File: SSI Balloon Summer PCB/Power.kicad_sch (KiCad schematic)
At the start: 35 parts, among them J1 Battery connector, Q2 DMG2305UX-7, SW1 SW_SPDT, U11 TPS63070RNMR, U12 TPS63070RNMR, U3 AP2112K-3.3TRG1

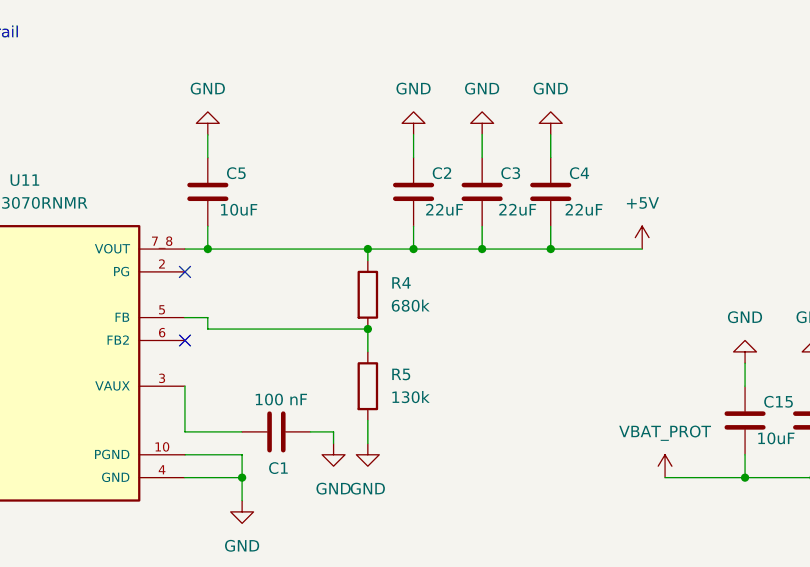
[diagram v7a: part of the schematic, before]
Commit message: Removed sketchy R4 footprint
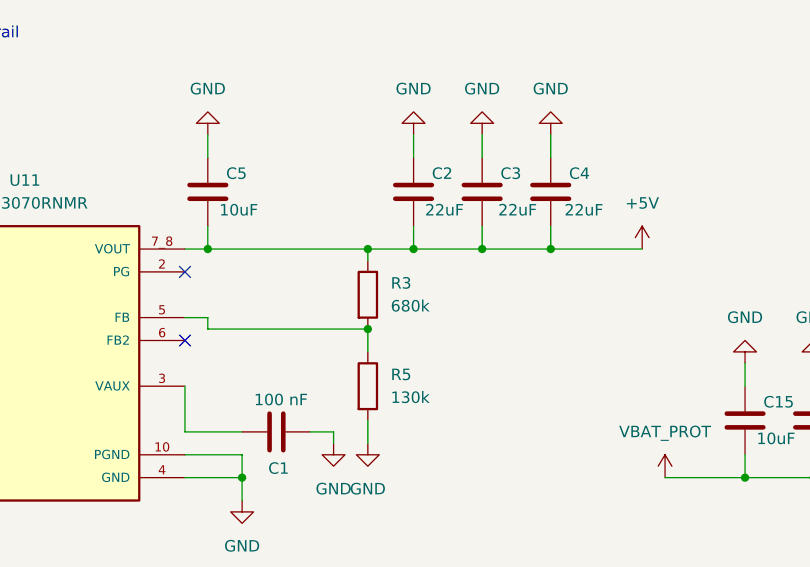
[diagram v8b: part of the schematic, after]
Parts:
- removed R4: 680k, AP2112K-3.3TRG1:SOT95P285X140-5N, symbol Device:R
- added R3: 680k, Resistor_SMD:R_0603_1608Metric, symbol Device:R
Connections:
- net +5V: now also R3.1
- net at R5.1, U11.5 (FB): now also R3.2
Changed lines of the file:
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@@
+	)
+	(junction
+		(at 120.65 102.87)
+		(diameter 0)
+		(color 0 0 0 0)
 	)
 	(junction
 		(at 233.68 144.78)
-		(diameter 0)
-		(color 0 0 0 0)
-	)
-	(junction
-		(at 120.65 102.87)
 		(diameter 0)
 		(color 0 0 0 0)
@@
 	)
 	(symbol
+		(lib_id "Device:R")
+		(at 120.65 99.06 0)
+		(unit 1)
+		(body_style 1)
+		(exclude_from_sim no)
+		(in_bom yes)
+		(on_board yes)
+		(in_pos_files yes)
+		(dnp no)
+		(fields_autoplaced yes)
+		(property "Reference" "R3"
+			(at 123.19 97.7899 0)
+			(show_name no)
+			(do_not_autoplace no)
+			(effects
+				(font
+					(size 1.27 1.27)
+				)
+				(justify left)
+			)
+		)
+		(property "Value" "680k"
+			(at 123.19 100.3299 0)
+			(show_name no)
+			(do_not_autoplace no)
+			(effects
+				(font
+					(size 1.27 1.27)
+				)
+				(justify left)
+			)
+		)
+		(property "Footprint" "Resistor_SMD:R_0603_1608Metric"
+			(at 118.872 99.06 90)
+			(hide yes)
+			(show_name no)
+			(do_not_autoplace no)
+			(effects
+				(font
+					(size 1.27 1.27)
+				)
+			)
+		)
+		(property "Datasheet" ""
+			(at 120.65 99.06 0)
+			(hide yes)
+			(show_name no)
+			(do_not_autoplace no)
+			(effects
+				(font
+					(size 1.27 1.27)
+				)
+			)
+		)
+		(property "Description" "Resistor"
+			(at 120.65 99.06 0)
+			(hide yes)
+			(show_name no)
+			(do_not_autoplace no)
+			(effects
+				(font
+					(size 1.27 1.27)
+				)
+			)
+		)
+		(pin "1"
+		)
+		(pin "2"
+		)
+		(instances
+			(project "SSI Summer Balloons"
+				(path "/3c45a535-6e6b-4825-ad52-82c10cbe7866/1b5737e2-4399-496a-b942-ad94430e2078"
+					(reference "R3")
+					(unit 1)
+				)
+			)
+		)
+	)
+	(symbol
 		(lib_id "Device:C")
 		(at 170.18 113.03 0)
@@
 					(unit 1)
 				)
-			)
-		)
-	)
-	(symbol
-		(lib_id "Device:R")
-		(at 120.65 99.06 0)
-		(unit 1)
-		(body_style 1)
-		(exclude_from_sim no)
-		(in_bom yes)
-		(on_board yes)
-		(in_pos_files yes)
-		(dnp no)
-		(fields_autoplaced yes)
-		(property "Reference" "R4"
-			(at 123.19 97.7899 0)
-			(show_name no)
-			(do_not_autoplace no)
-			(effects
-				(font
-					(size 1.27 1.27)
-				)
-				(justify left)
-			)
-		)
-		(property "Value" "680k"
-			(at 123.19 100.3299 0)
-			(show_name no)
-			(do_not_autoplace no)
-			(effects
-				(font
-					(size 1.27 1.27)
-				)
-				(justify left)
-			)
-		)
-		(property "Footprint" "AP2112K-3.3TRG1:SOT95P285X140-5N"
-			(at 118.872 99.06 90)
-			(hide yes)
-			(show_name no)
-			(do_not_autoplace no)
-			(effects
-				(font
-					(size 1.27 1.27)
-				)
-			)
-		)
-		(property "Datasheet" ""
-			(at 120.65 99.06 0)
-			(hide yes)
-			(show_name no)
-			(do_not_autoplace no)
-			(effects
-				(font
-					(size 1.27 1.27)
-				)
-			)
-		)
-		(property "Description" "Voltage Regulators, LDO, 600mA CMOS LDO 50mA 3.3V 250mV | Diodes Inc AP2112K-3.3TRG1"
-			(at 120.65 99.06 0)
-			(hide yes)
-			(show_name no)
-			(do_not_autoplace no)
-			(effects
-				(font
-					(size 1.27 1.27)
-				)
-			)
-		)
-		(property "Availability" "In Stock"
-			(at 120.65 99.06 0)
-			(hide yes)
-			(show_name no)
-			(do_not_autoplace no)
-			(effects
-				(font
-					(size 1.27 1.27)
-				)
-			)
-		)
-		(property "Check_prices" "https://www.snapeda.com/parts/AP2112K-3.3TRG1/Diodes+Inc./view-part/?ref=eda"
-			(at 120.65 99.06 0)
-			(hide yes)
-			(show_name no)
-			(do_not_autoplace no)
-			(effects
-				(font
-					(size 1.27 1.27)
-				)
-			)
-		)
-		(property "MANUFACTURER" "Diodes Inc."
-			(at 120.65 99.06 0)
-			(hide yes)
-			(show_name no)
-			(do_not_autoplace no)
-			(effects
-				(font
-					(size 1.27 1.27)
-				)
-			)
-		)
-		(property "MF" "Diodes Inc."
-			(at 120.65 99.06 0)
-			(hide yes)
-			(show_name no)
-			(do_not_autoplace no)
-			(effects
-				(font
-					(size 1.27 1.27)
-				)
-			)
-		)
-		(property "MP" "AP2112K-3.3TRG1"
-			(at 120.65 99.06 0)
-			(hide yes)
-			(show_name no)
-			(do_not_autoplace no)
-			(effects
-				(font
-					(size 1.27 1.27)
-				)
-			)
-		)
-		(property "PARTREV" "2-2"
-			(at 120.65 99.06 0)
-			(hide yes)
-			(show_name no)
-			(do_not_autoplace no)
-			(effects
-				(font
-					(size 1.27 1.27)
-				)
-			)
-		)
-		(property "Package" "SOT-753 Diodes Inc."
-			(at 120.65 99.06 0)
-			(hide yes)
-			(show_name no)
-			(do_not_autoplace no)
-			(effects
-				(font
-					(size 1.27 1.27)
-				)
-			)
-		)
-		(property "Price" "None"
-			(at 120.65 99.06 0)
-			(hide yes)
-			(show_name no)
-			(do_not_autoplace no)
-			(effects
-				(font
-					(size 1.27 1.27)
-				)
-			)
-		)
-		(property "SnapEDA_Link" "https://www.snapeda.com/parts/AP2112K-3.3TRG1/Diodes+Inc./view-part/?ref=snap"
-			(at 120.65 99.06 0)
-			(hide yes)
-			(show_name no)
-			(do_not_autoplace no)
-			(effects
-				(font
-					(size 1.27 1.27)
-				)
-			)
-		)
-		(pin "2"
-		)
-		(pin "1"
-		)
-		(instances
-			(project "SSI Summer Balloons"
-				(path "/3c45a535-6e6b-4825-ad52-82c10cbe7866/1b5737e2-4399-496a-b942-ad94430e2078"
-					(reference "R4")
-					(unit 1)
-				)
